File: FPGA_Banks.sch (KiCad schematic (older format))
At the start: 37 parts

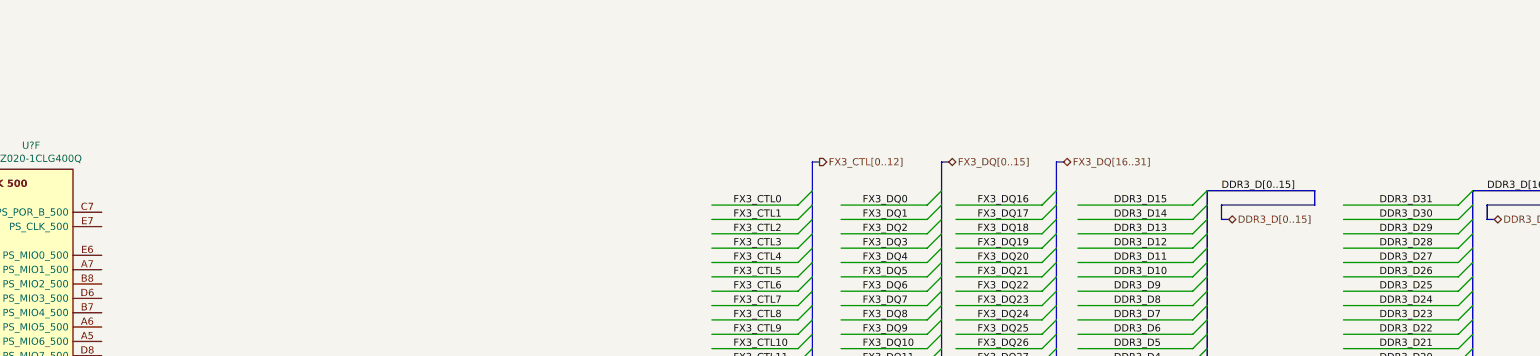
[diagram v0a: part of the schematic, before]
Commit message: -Clock --GND pin was missing. it was added to pin 45 -BTB --pins added
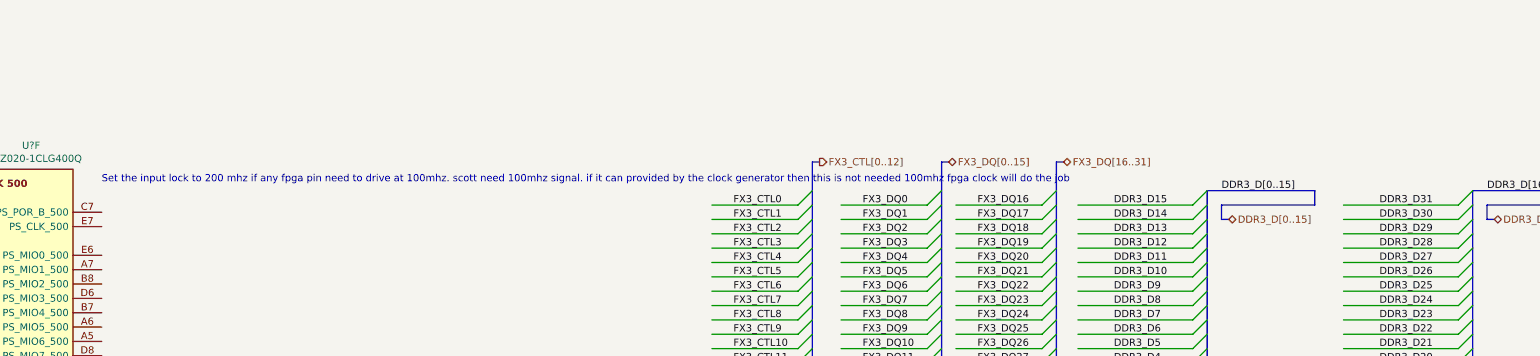
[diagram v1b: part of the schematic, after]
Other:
- note added: "Set the input lock to 200 mhz if any fpga pin need to drive at 100mhz. scott need 100mhz signal. if it can provided by the clock generator then this is not needed 100mhz fpga clock will do the job\n"
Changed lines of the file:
@@
 $Descr A3 16535 11693
 encoding utf-8
-Sheet 23 25
+Sheet 25 25
 Title ""
 Date ""
@@
 Wire Bus Line
 	12250 7900 12250 9600
+Text Notes 5600 8050 0    50   ~ 0
+Set the input lock to 200 mhz if any fpga pin need to drive at 100mhz. scott need 100mhz signal. if it can provided by the clock generator then this is not needed 100mhz fpga clock will do the job\n
 $EndSCHEMATC

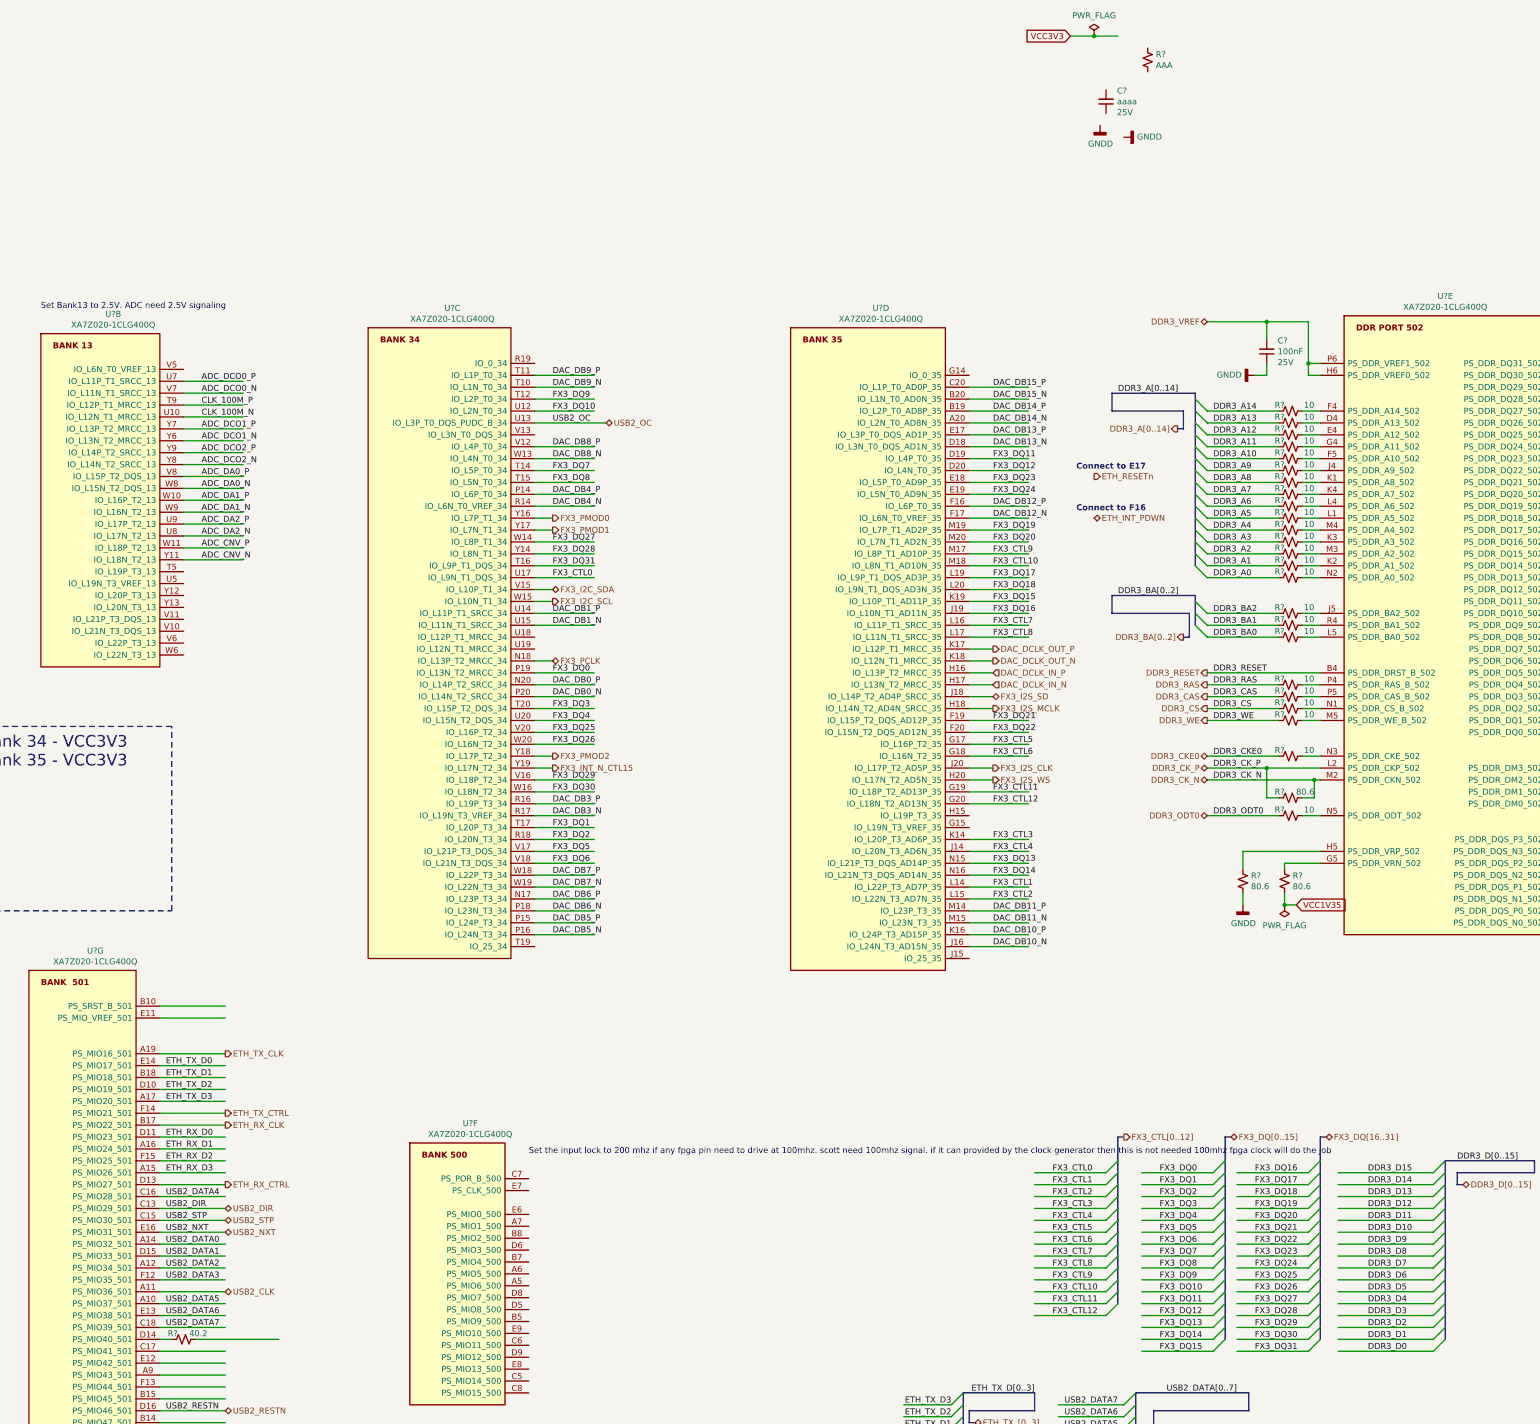
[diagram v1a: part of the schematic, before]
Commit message: PCB created and schematics annotated High speed connections added to the BTB
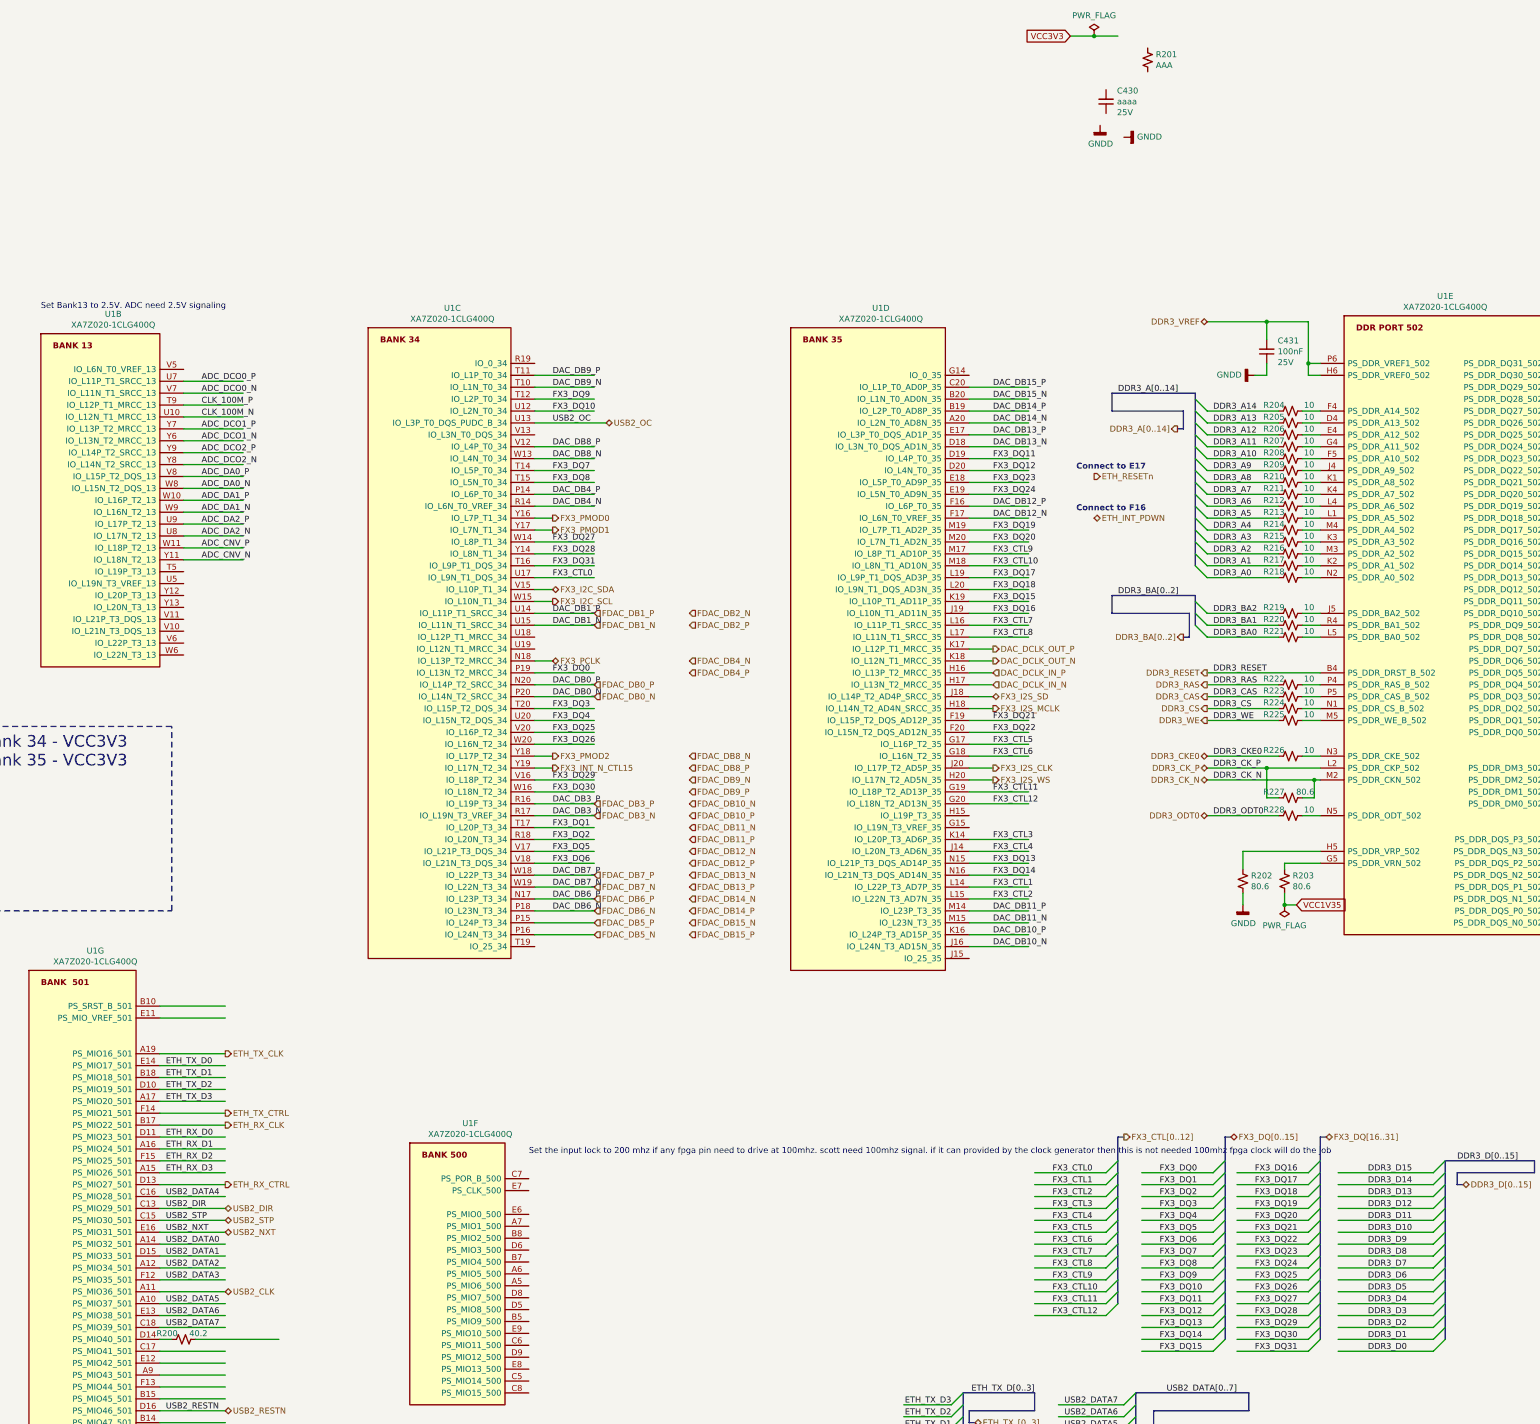
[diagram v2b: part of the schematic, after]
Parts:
- gave numbers to parts that had none: 32
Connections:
- net labels added: FDAC_DB0_N, FDAC_DB0_P, FDAC_DB10_N, FDAC_DB10_P, FDAC_DB11_N, FDAC_DB11_P, FDAC_DB12_N, FDAC_DB12_P, FDAC_DB13_N, FDAC_DB13_P, FDAC_DB14_N, FDAC_DB14_P, FDAC_DB15_N, FDAC_DB15_P, FDAC_DB1_N, FDAC_DB1_P, FDAC_DB2_N, FDAC_DB2_P, FDAC_DB3_N, FDAC_DB3_P, FDAC_DB4_N, FDAC_DB4_P, FDAC_DB5_N, FDAC_DB5_P, FDAC_DB6_N, FDAC_DB6_P, FDAC_DB7_N, FDAC_DB7_P, FDAC_DB8_N, FDAC_DB8_P, FDAC_DB9_N, FDAC_DB9_P
- net labels removed: DAC_DB5_N, DAC_DB5_P

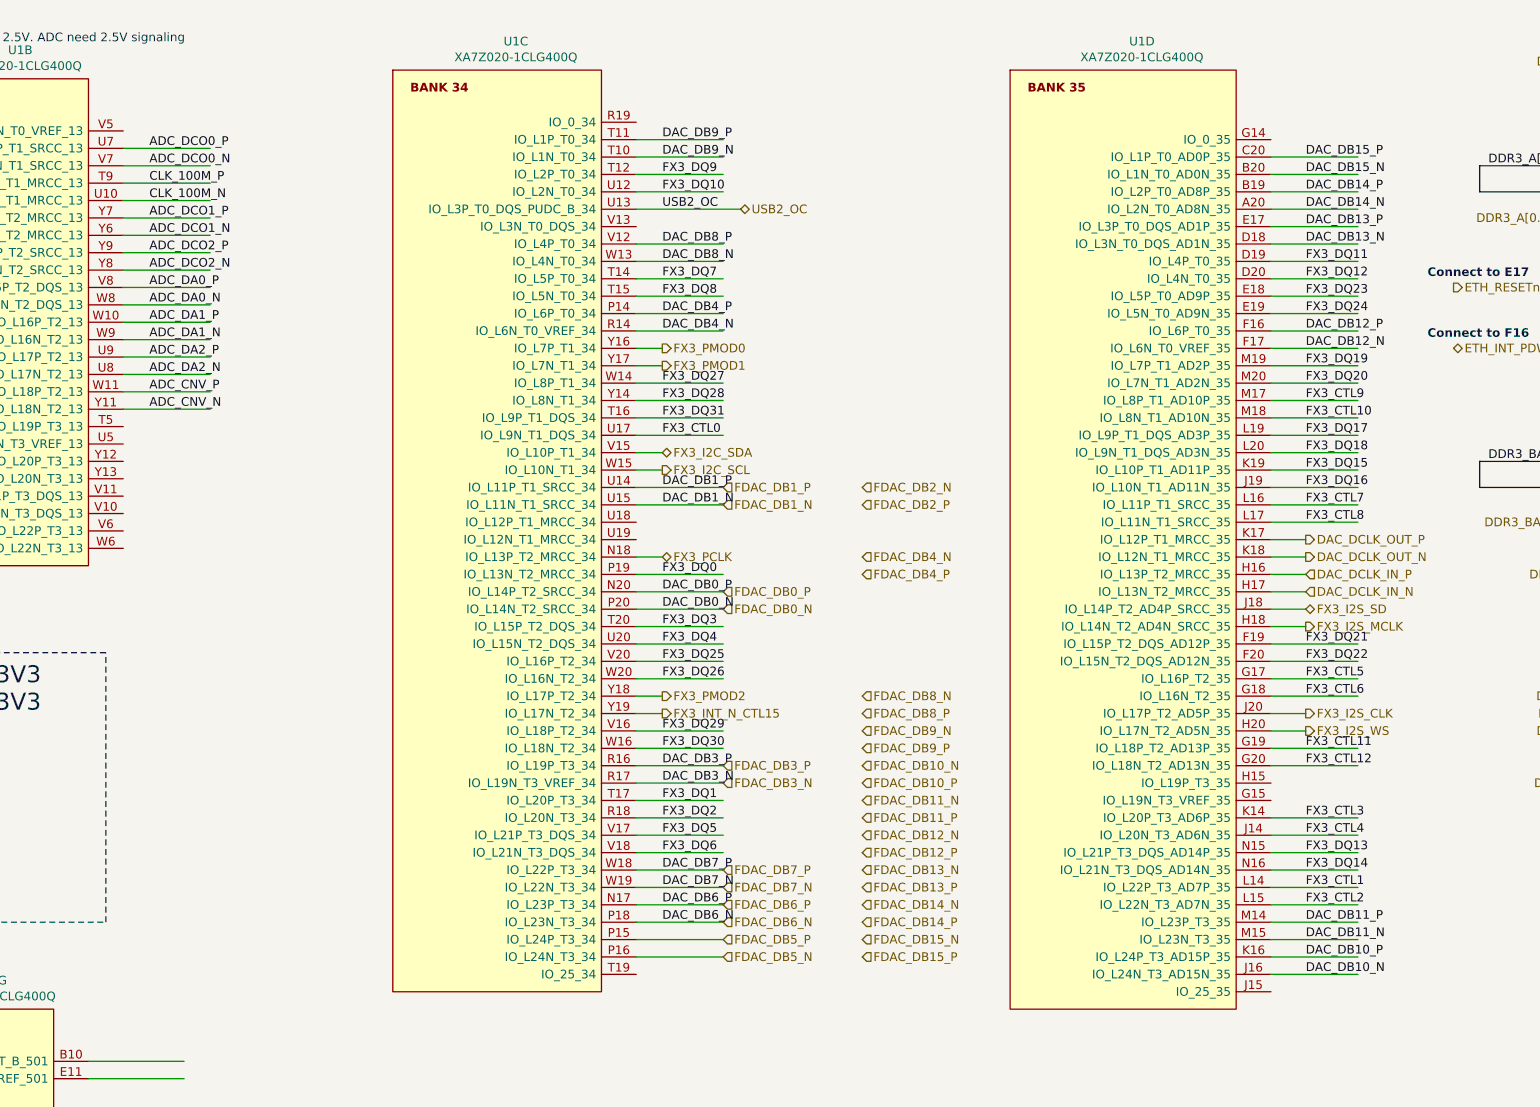
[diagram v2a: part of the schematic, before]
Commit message: BTB and FPGA pins added and connections were made
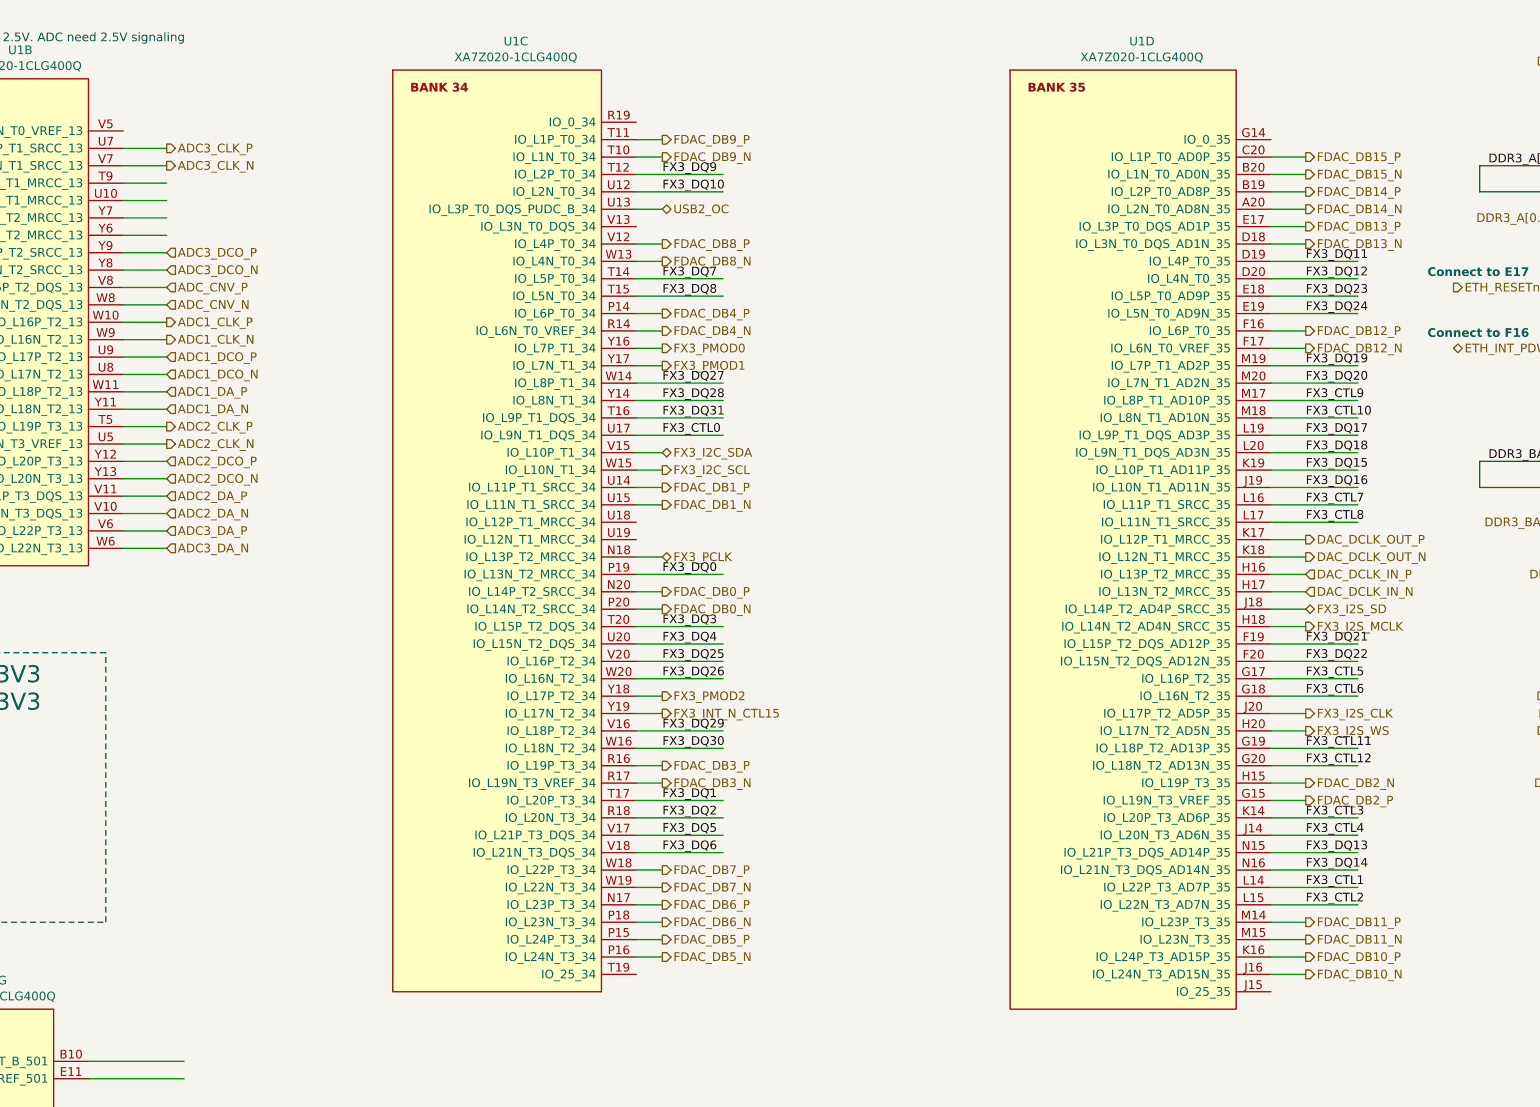
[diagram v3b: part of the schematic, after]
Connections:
- net labels added: ADC1_CLK_N, ADC1_CLK_P, ADC1_DA_N, ADC1_DA_P, ADC1_DCO_N, ADC1_DCO_P, ADC2_CLK_N, ADC2_CLK_P, ADC2_DA_N, ADC2_DA_P, ADC2_DCO_N, ADC2_DCO_P, ADC3_CLK_N, ADC3_CLK_P, ADC3_DA_N, ADC3_DA_P, ADC3_DCO_N, ADC3_DCO_P
- net labels removed: ADC_DA0_N, ADC_DA0_P, ADC_DA1_N, ADC_DA1_P, ADC_DA2_N, ADC_DA2_P, ADC_DCO0_N, ADC_DCO0_P, ADC_DCO1_N, ADC_DCO1_P, ADC_DCO2_N, ADC_DCO2_P, CLK_100M_N, CLK_100M_P, DAC_DB0_N, DAC_DB0_P, DAC_DB10_N, DAC_DB10_P, DAC_DB11_N, DAC_DB11_P, DAC_DB12_N, DAC_DB12_P, DAC_DB13_N, DAC_DB13_P, DAC_DB14_N, DAC_DB14_P, DAC_DB15_N, DAC_DB15_P, DAC_DB1_N, DAC_DB1_P, DAC_DB3_N, DAC_DB3_P, DAC_DB4_N, DAC_DB4_P, DAC_DB6_N, DAC_DB6_P, DAC_DB7_N, DAC_DB7_P, DAC_DB8_N, DAC_DB8_P, DAC_DB9_N, DAC_DB9_P
- wire segments 360 -> 370
